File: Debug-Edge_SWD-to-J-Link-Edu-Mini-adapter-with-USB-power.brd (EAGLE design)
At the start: 29.2 x 10.2 mm, 8 parts, among them J1 AVX_6-PIN_009159006061916, J3 CORTEX_DEBUG_PTH, J4 2172034-1

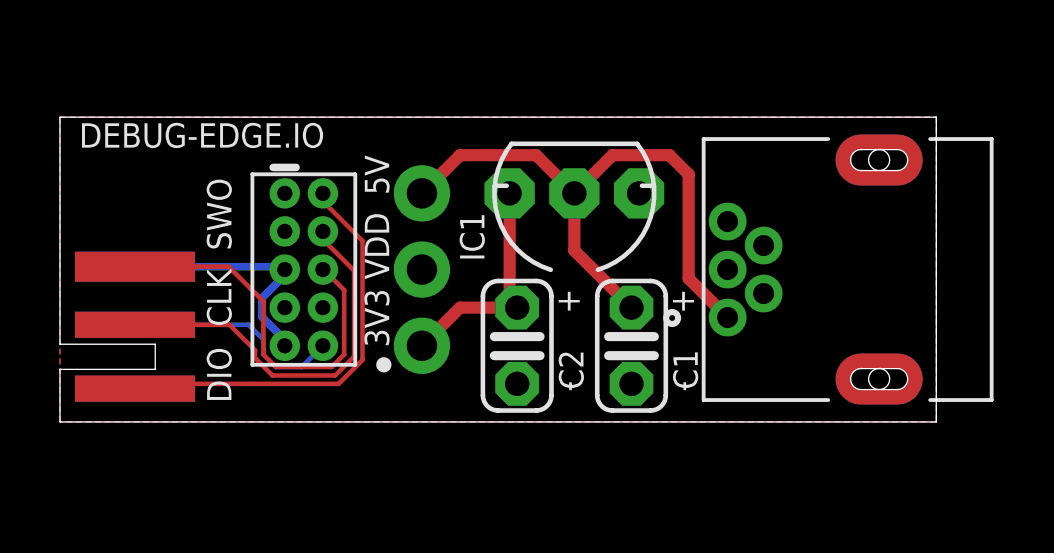
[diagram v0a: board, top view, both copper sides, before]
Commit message: Updated footprint for USB connector.
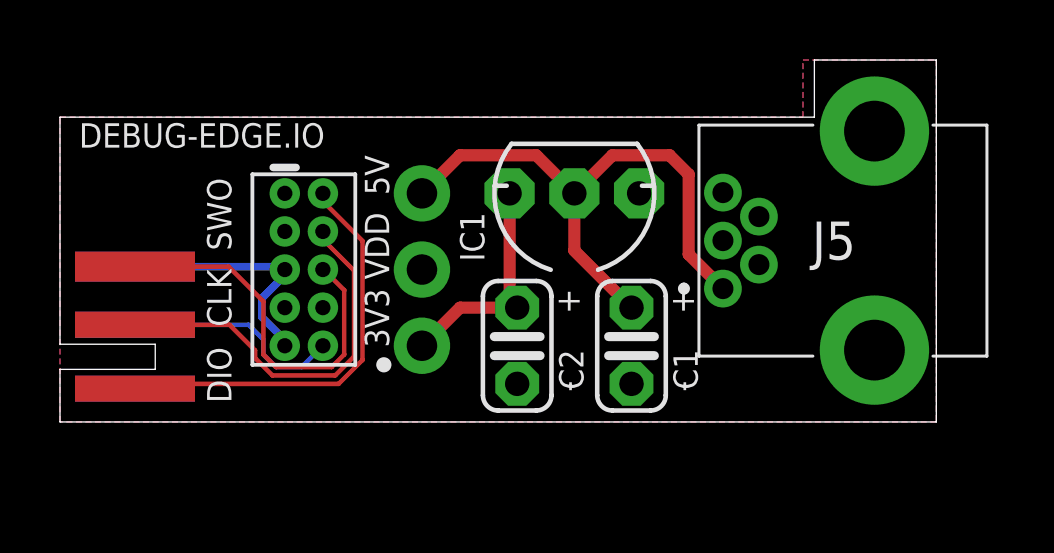
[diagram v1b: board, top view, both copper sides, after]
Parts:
- removed J4: 2172034-1, USB-mini-B_TE_2172034-1:TE_2172034-1
- added J5: 2172034-1, 2172034-1:21720341
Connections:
- net 5V: now also J5.1; no longer J4.1
- net GND: now also J5.4, J5.5, J5.MH1, J5.MH2; no longer J4.5, J4.SH1, J4.SH2
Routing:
- net 5V: track 20.6 -> 19.6 mm
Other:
- board size 29.2 x 10.2 mm -> 29.2 x 12.1 mm
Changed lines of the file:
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@@
 <layers>
 <layer number="1" name="Top" color="4" fill="1" visible="yes" active="yes"/>
-<layer number="16" name="Bottom" color="1" fill="1" visible="no" active="yes"/>
+<layer number="16" name="Bottom" color="1" fill="1" visible="yes" active="yes"/>
 <layer number="17" name="Pads" color="2" fill="1" visible="yes" active="yes"/>
 <layer number="18" name="Vias" color="2" fill="1" visible="yes" active="yes"/>
@@
 <plain>
 <wire x1="0" y1="0" x2="29.21" y2="0" width="0" layer="20"/>
-<wire x1="29.21" y1="0" x2="29.21" y2="10.16" width="0" layer="20"/>
-<wire x1="29.21" y1="10.16" x2="0" y2="10.16" width="0" layer="20"/>
 <text x="10.16" y="4.445" size="0.8128" layer="25" ratio="6" rot="R270">3V3</text>
 <text x="10.16" y="6.985" size="0.8128" layer="25" ratio="6" rot="R270">VDD</text>
@@
 <text x="16.51" y="4.445" size="0.8128" layer="25" ratio="6" rot="R270">-       +</text>
 <dimension x1="0" y1="0" x2="0" y2="10.16" x3="-1.27" y3="5.08" textsize="1.778" layer="51" unit="inch"/>
-<dimension x1="0" y1="10.16" x2="29.21" y2="10.16" x3="14.605" y3="11.43" textsize="1.778" layer="51" unit="inch"/>
+<wire x1="0" y1="10.16" x2="25.146" y2="10.16" width="0.000203125" layer="20"/>
+<wire x1="25.146" y1="10.16" x2="25.146" y2="12.065" width="0.000203125" layer="20"/>
+<wire x1="25.146" y1="12.065" x2="29.21" y2="12.065" width="0.000203125" layer="20"/>
+<wire x1="29.21" y1="12.065" x2="29.21" y2="0" width="0.000203125" layer="20"/>
+<dimension x1="0" y1="10.16" x2="29.21" y2="10.16" x3="14.605" y3="13.335" textsize="1.778" layer="51" unit="inch"/>
+<dimension x1="29.21" y1="12.065" x2="29.21" y2="0" x3="34.925" y3="6.0325" textsize="1.778" layer="51" unit="inch"/>
 </plain>
 <attributes>
@@
 <attribute name="VALUE" x="5.6642" y="6.9088" size="0.6096" layer="27" font="vector" ratio="20" rot="R270"/>
 </element>
-<element name="J4" library="USB-mini-B_TE_2172034-1" package="TE_2172034-1" value="2172034-1" x="27.305" y="5.08" smashed="yes">
-<attribute name="COMMENT" value="2172034-1" x="27.305" y="5.08" size="1.778" layer="27" display="off"/>
-<attribute name="DESCRIPTION" value=" Conn Mini USB Type B RCP 5 POS 0.8mm Solder RA Thru-Hole 5 Terminal 1 Port Box/Tray " x="27.305" y="5.08" size="1.778" layer="27" display="off"/>
-<attribute name="DIGI-KEY_PART_NUMBER" value="A135698-ND" x="27.305" y="5.08" size="1.778" layer="27" display="off"/>
-<attribute name="EU_ROHS_COMPLIANCE" value="Compliant" x="27.305" y="5.08" size="1.778" layer="27" display="off"/>
-<attribute name="MF" value="TE Connectivity" x="27.305" y="5.08" size="1.778" layer="27" display="off"/>
-<attribute name="MP" value="2172034-1" x="27.305" y="5.08" size="1.778" layer="27" display="off"/>
-<attribute name="PACKAGE" value="None" x="27.305" y="5.08" size="1.778" layer="27" display="off"/>
-<attribute name="PURCHASE-URL" value="https://pricing.snapeda.com/search/part/2172034-1/?ref=eda" x="27.305" y="5.08" size="1.778" layer="27" display="off"/>
-<attribute name="VALUE" x="20.824240625" y="-2.055840625" size="1.778209375" layer="27"/>
-</element>
 <element name="IC1" library="adafruit" package="TO92-INLINE" value="" x="17.145" y="7.62" smashed="yes" rot="R180">
 <attribute name="NAME" x="13.335" y="6.985" size="0.8128" layer="25" ratio="6" rot="R270"/>
@@
 <attribute name="VALUE" x="12.573" y="4.318" size="1.27" layer="27" ratio="10" rot="R270"/>
 </element>
+<element name="J5" library="2172034-1" package="21720341" value="2172034-1" x="22.098" y="4.445" smashed="yes">
+<attribute name="ARROW_PART_NUMBER" value="2172034-1" x="22.098" y="4.445" size="1.778" layer="27" display="off"/>
+<attribute name="ARROW_PRICE-STOCK" value="https://www.arrow.com/en/products/2172034-1/te-connectivity" x="22.098" y="4.445" size="1.778" layer="27" display="off"/>
+<attribute name="DESCRIPTION" value="CONN RCPT USB MINI B 2.0 PCB R/A" x="22.098" y="4.445" size="1.778" layer="27" display="off"/>
+<attribute name="HEIGHT" value="3.9mm" x="22.098" y="4.445" size="1.778" layer="27" display="off"/>
+<attribute name="MANUFACTURER_NAME" value="TE Connectivity" x="22.098" y="4.445" size="1.778" layer="27" display="off"/>
+<attribute name="MANUFACTURER_PART_NUMBER" value="2172034-1" x="22.098" y="4.445" size="1.778" layer="27" display="off"/>
+<attribute name="MOUSER_PART_NUMBER" value="571-2172034-1" x="22.098" y="4.445" size="1.778" layer="27" display="off"/>
+<attribute name="MOUSER_PRICE-STOCK" value="https://www.mouser.co.uk/ProductDetail/TE-Connectivity/2172034-1/?qs=Ev%252BS503VEAHBC%252BPBdsvCGg%3D%3D" x="22.098" y="4.445" size="1.778" layer="27" display="off"/>
+<attribute name="NAME" x="25.798" y="6.045" size="1.27" layer="25" align="center"/>
+<attribute name="VALUE" x="25.798" y="6.045" size="1.27" layer="27" align="center"/>
+</element>
 </elements>
 <signals>
 <signal name="GND">
-<polygon width="0.254" layer="1">
-<vertex x="0" y="0"/>
-<vertex x="0" y="10.16"/>
-<vertex x="29.21" y="10.16"/>
-<vertex x="29.21" y="0"/>
-</polygon>
 <contactref element="J3" pad="3"/>
-<contactref element="J4" pad="5"/>
 <contactref element="C1" pad="2"/>
 <contactref element="J3" pad="5"/>
 <contactref element="J3" pad="9"/>
-<contactref element="J4" pad="SH1"/>
-<contactref element="J4" pad="SH2"/>
 <contactref element="IC1" pad="1"/>
 <contactref element="C2" pad="2"/>
@@
 <wire x1="7.493" y1="2.73236875" x2="6.731" y2="3.49436875" width="0.254" layer="16"/>
 <wire x1="6.731" y1="4.12563125" x2="7.493" y2="4.88763125" width="0.254" layer="16"/>
-<wire x1="22.255" y1="6.68" x2="26.035" y2="8.89" width="0" layer="19" extent="1-1"/>
-<wire x1="26.035" y1="1.27" x2="22.255" y2="6.68" width="0" layer="19" extent="1-1"/>
+<contactref element="J5" pad="4"/>
+<contactref element="J5" pad="5"/>
+<contactref element="J5" pad="MH1"/>
+<contactref element="J5" pad="MH2"/>
+<polygon width="0.000203125" layer="1">
+<vertex x="0" y="0"/>
+<vertex x="0" y="10.16"/>
+<vertex x="24.765" y="10.16"/>
+<vertex x="24.765" y="12.065"/>
+<vertex x="29.21" y="12.065"/>
+<vertex x="29.21" y="0"/>
+</polygon>
 </signal>
 <signal name="5V">
 <contactref element="J2" pad="3"/>
 <contactref element="C1" pad="1"/>
-<contactref element="J4" pad="1"/>
 <contactref element="IC1" pad="2"/>
-<wire x1="22.255" y1="3.48" x2="20.955" y2="4.78" width="0.4064" layer="1"/>
-<wire x1="20.955" y1="4.78" x2="20.955" y2="8.255" width="0.4064" layer="1"/>
-<wire x1="20.955" y1="8.255" x2="20.32" y2="8.89" width="0.4064" layer="1"/>
+<wire x1="20.32" y1="8.89" x2="20.955" y2="8.255" width="0.4064" layer="1"/>
 <wire x1="20.32" y1="8.89" x2="18.415" y2="8.89" width="0.4064" layer="1"/>
 <wire x1="18.415" y1="8.89" x2="17.145" y2="7.62" width="0.4064" layer="1"/>
@@
 <wire x1="15.875" y1="8.89" x2="13.335" y2="8.89" width="0.4064" layer="1"/>
 <wire x1="13.335" y1="8.89" x2="12.065" y2="7.62" width="0.4064" layer="1"/>
+<contactref element="J5" pad="1"/>
+<wire x1="20.955" y1="5.588" x2="22.098" y2="4.445" width="0.4064" layer="1"/>
+<wire x1="20.955" y1="8.255" x2="20.955" y2="5.588" width="0.4064" layer="1"/>
 </signal>
 <signal name="3V3">
@@
 </signal>
 <signal name="VTREF">
-<polygon width="0.254" layer="16">
-<vertex x="0" y="0"/>
-<vertex x="0" y="10.16"/>
-<vertex x="29.21" y="10.16"/>
-<vertex x="29.21" y="0"/>
-</polygon>
 <contactref element="J2" pad="2"/>
 <contactref element="J3" pad="1"/>
 <contactref element="J1" pad="1"/>
+<polygon width="0.000203125" layer="16">
+<vertex x="0" y="0"/>
+<vertex x="0" y="10.16"/>
+<vertex x="24.765" y="10.16"/>
+<vertex x="24.765" y="12.065"/>
+<vertex x="29.21" y="12.065"/>
+<vertex x="29.21" y="0"/>
+</polygon>
 </signal>
 <signal name="SWDIO">
